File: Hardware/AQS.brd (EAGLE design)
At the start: 70 x 60 mm, 43 parts, among them IC1 BME680, IC2 CP2102N-A01-GQFN24, IC4 ESPWROOM32, J1 ESP-PROG-2X3-1.27-SHROUDED, J2 M02X5-1.27-S, J3 USB-C-16P-16P, Q1 MMDT3904, Q2 2N7002

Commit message: Finished major rework for v3.0 release
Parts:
- removed IC4: ESPWROOM32, SuperHouse-MCUs:ESPWROOM32
- added IC3: BME680, SuperHouse-Sensors:BME680
- added U$23, U$24, U$25: FIDUCIAL1X2, SuperHouse-Symbols:FIDUCIAL-1X2
- C2, C3: device SuperHouse-DiscreteSemi:C0603 -> SuperHouse-DiscreteSemi:C0805
- C5: value 10uF 50V -> 10uF
- IC1: value BME680 -> ESPWROOM32; device SuperHouse-Sensors:BME680 -> SuperHouse-MCUs:ESPWROOM32
- LED2: value WS2812B5050 -> TX/YEL; device SuperHouse-LEDs:WS2812B -> SuperHouse-LEDs:LED-0603
- LED5: value TX/YEL -> WS2812B5050; device SuperHouse-LEDs:LED-0603 -> SuperHouse-LEDs:WS2812B
- R1: value 10K -> 1K
- R10: value 5.1K -> 10K
- R11: value 22K -> 10K
- R13: value 4K7 -> 22K
- R14: value 4K7 -> 22.1K
- R15: value 4K7 -> 47.5K
- R2: value 22.1K -> 1K
- R3: value 47.5K -> 4K7
- R5: value 10K -> 4K7
- R6: value 5.1K -> 4K7
- R7: value 10K -> 5.1K
- R8: value 1K -> 5.1K
- R9: value 1K -> 10K
- moved R5 69.3 mm to (63.5, 13.0), turned to 0 degrees
- moved LED5 60.2 mm to (64.0, 51.0)
- moved LED4 58.0 mm to (6.00, 51.0)
- moved R15 55.9 mm to (9.00, 25.5), turned to 270 degrees
- moved R14 55.5 mm to (9.00, 21.5), turned to 270 degrees
- moved R11 54.0 mm to (7.00, 45.0), turned to 270 degrees
- moved R6 53.7 mm to (63.5, 11.0), turned to 0 degrees
- moved R13 53.6 mm to (61.0, 45.5)
- moved R1 46.1 mm to (5.00, 29.0), turned to 90 degrees
- moved R9 46.1 mm to (40.0, 59.0), turned to 0 degrees
- moved IC1 44.1 mm to (16.5, 55.0), flipped to the bottom, turned to 0 degrees
- moved R10 35.9 mm to (2.00, 45.0), turned to 90 degrees
- moved R3 30.5 mm to (8.50, 56.5), turned to 90 degrees
- moved R7 29.2 mm to (10.0, 16.0), turned to 180 degrees
- moved R8 19.2 mm to (10.0, 10.0), turned to 180 degrees
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- renumbered C12 to C7, LED6 to LED3
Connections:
- removed net GPIO13: IC4.16, Q2.2, R4.1
- removed net GPIO2: IC4.24, LCD.DC
- removed net GPIO23: IC4.37
- removed net GPIO4: IC4.26
- removed net TFT_CIPO: IC4.31
- removed net TFT_CS: IC4.11
- removed net TFT_RESET: LCD.RES
- new net TFT_DC: IC1.24, LCD.DC
- new net TFT_RST: IC1.26, LCD.RES
- new net WS2812B: IC1.16, Q2.2, R4.1
- net !RESET: now also IC1.3, R13.2; no longer IC4.3, R11.2
- net 3.3V: now also IC3.2, IC3.6, IC3.8, LED2.A, R13.1, R5.2, R6.2, R9.2; no longer IC1.6, IC1.8, IC4.2, LED5.A, R1.2, R11.1, R14.2, R15.2
- net 5V: now also LED5.1-VDD, R14.2, R3.2; no longer LED2.1-VDD, R13.2, R2.2
- net DTR: now also R10.1; no longer R5.1
- net GND: now also IC1.15, IC1.38, IC1.GND@4, IC3.1, IC3.5, IC3.7, LED5.3-GND, R15.1, R7.1, R8.1; no longer IC1.5, IC1.7, IC4.1, IC4.15, IC4.38, IC4.GND@4, LED2.3-GND, R10.1, R3.1, R6.1
- net GPIO0: now also IC1.25; no longer IC4.25
- net H1: now also LED4.4-DIN, R3.1; no longer LED2.4-DIN, R13.1
- net N$1: now also R9.1; no longer R1.1
- net N$10: now also R8.2; no longer R10.2
- net N$11: now also R7.2; no longer R6.2
- net N$12: now also LED4.2-DOUT, LED5.4-DIN; no longer LED2.2-DOUT, LED4.4-DIN
- net N$13: now also LED2.C, R1.2; no longer LED5.C, R9.2
- net N$2: now also R2.2; no longer R8.2
- net N$39: now also R14.1, R15.2; no longer R2.1, R3.2
- net N$7: now also R10.2; no longer R5.2
- net N$8: now also R11.2; no longer R7.2
- net PMS_RESET: now also IC1.12; no longer IC4.12
- net PMS_RX: now also IC1.28; no longer IC4.28
- net PMS_SET: now also IC1.10; no longer IC4.10
- net PMS_TX: now also IC1.27; no longer IC4.27
- net RTS: now also R11.1; no longer R7.1
- net RXD0: now also IC1.34; no longer IC4.34
- net RX_LED: now also R2.1; no longer R8.1
- net SCL: now also IC1.36, IC3.4, R6.1; no longer IC1.4, IC4.36, R14.1
- net SDA: now also IC1.33, IC3.3, R5.1; no longer IC1.3, IC4.33, R15.1
- net TFT_COPI: now also IC1.37
- net TFT_SCLK: now also IC1.30; no longer IC4.30
- net TXD0: now also IC1.35; no longer IC4.35
- net TX_LED: now also R1.1; no longer R9.1
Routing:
- net GPIO2: track 56.5 -> 0.00 mm, vias 2 -> 0
- net TFT_RST: track 0.00 -> 55.8 mm, vias 0 -> 1
- net TFT_DC: track 0.00 -> 54.1 mm, vias 0 -> 1
- net GPIO4: track 50.5 -> 0.00 mm, vias 2 -> 0
- net TFT_COPI: track 0.00 -> 32.1 mm, vias 0 -> 1
- net WS2812B: track 0.00 -> 32.0 mm, vias 0 -> 3
- net GPIO23: track 29.9 -> 0.00 mm, vias 2 -> 0
- net PMS_TX: track 43.9 -> 17.0 mm, vias 2 -> 1
- net SDA: track 59.8 -> 85.9 mm, vias 1 -> 3
- net SCL: track 68.7 -> 92.9 mm, vias 1 -> 3
- net PMS_RESET: track 38.6 -> 29.1 mm
- net PMS_RX: track 15.1 -> 21.9 mm, vias 0 -> 1
- net 3.3V: track 51.4 -> 57.1 mm
- net PMS_SET: track 20.0 -> 23.9 mm, vias 1 -> 0
- net !RESET: track 83.1 -> 85.5 mm
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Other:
- board text added: "Pin Assignments: GPIO0: Button (active low) GPIO1: USB_TX GPIO2: TFT_DC GPIO3: USB_RX GPIO4: TFT_RST GPIO13: WS2812B GPIO16: PMS_TX (RX2 of MCU) GPIO17: PMS_RX (TX2 of MCU) GPIO18: TFT_SCLK GPIO21: SDA GPIO22: SCL GPIO23: TFT_COPI GPIO25: PMS_SET GPIO27: PMS_RESET"
- board text added: "v3.0"
- board text removed: "Pin Assignments: GPIO0: Button GPIO2: TFT_DC GPIO4: TFT_RST GPIO12: Tx to PMS7003 Rx GPIO14: PMS7003 SET GPIO15: TFT_CS GPIO16: WS2812B GPIO17: Rx from PMS7003 Tx GPIO18: TFT_SCLK GPIO19: TFT_MISO GPIO23: TFT_MOSI GPIO25: SDA GPIO26: SCL GPIO27: PMS7003 RESET"
- board text removed: "v2.0"

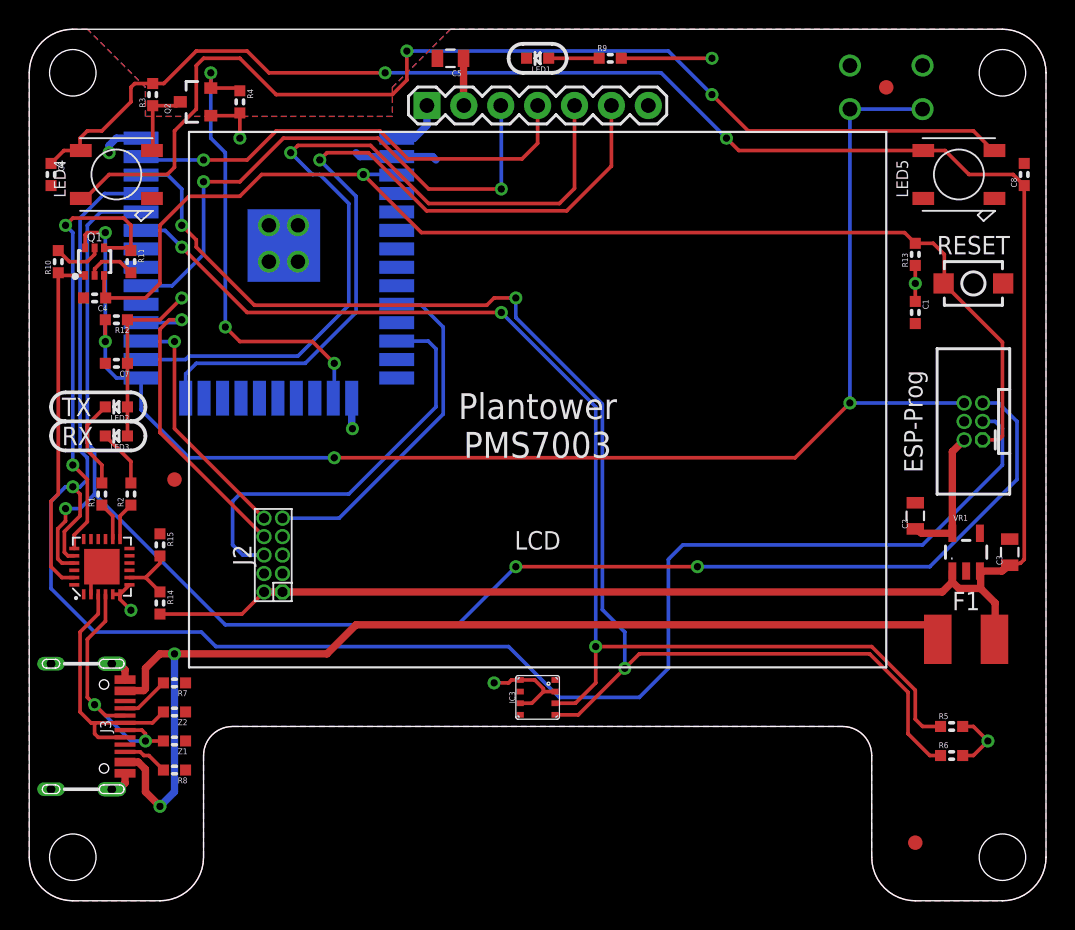
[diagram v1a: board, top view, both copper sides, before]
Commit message: Major restructure to reduce size of PCB. ERC and DRC for v3.0 release.
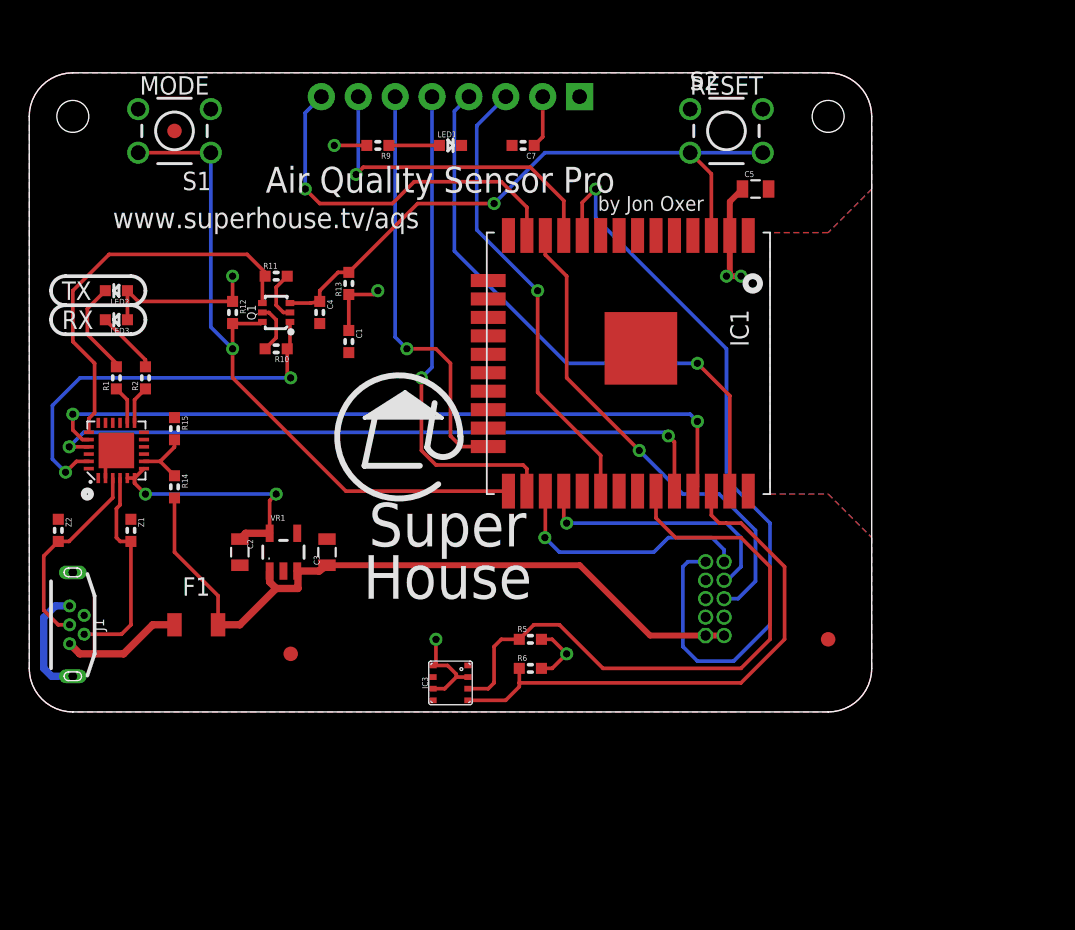
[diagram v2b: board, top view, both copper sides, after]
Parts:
- removed C6, C8: 100nF, SuperHouse-DiscreteSemi:C0603
- removed J3: USB-C-16P-16P, SuperHouse-Connectors:USB-C-16P
- removed LCD: OLED-SPI-HEADER, SuperHouse-Displays:OLED-240X240-1.3-HEADER
- removed LED4, LED5: WS2812B5050, SuperHouse-LEDs:WS2812B
- removed Q2: 2N7002, SuperHouse-DiscreteSemi:SOT23-3
- removed R3, R4: 4K7, SuperHouse-DiscreteSemi:R0603
- removed R7, R8: 5.1K, SuperHouse-DiscreteSemi:R0603
- added MOD1: OLED-SPI-CS-PINS, SuperHouse-Displays:OLED-240X240-1.54
- F1: device SuperHouse-Fuses:1812 -> SuperHouse-Fuses:1206
- J1: value ESP-PROG-2X3-1.27-SHROUDED -> USB; device SuperHouse-ESP-Prog:2X3-1.27-SHROUDED -> SuperHouse-Connectors:USB-MICROB-VERT
- S2: device SuperHouse-Switches:TACTILE_SMT_3X4X2 -> SuperHouse-Switches:TACTILE-PTH-4.5MM
- moved J1 63.6 mm to (3.00, 20.0)
- moved F1 53.0 mm to (11.5, 20.0)
- moved S1 49.1 mm to (10.0, 54.0), flipped to the top
- moved U$23 49.1 mm to (10.0, 54.0)
- moved C3 47.0 mm to (20.5, 25.0)
- moved VR1 47.0 mm to (17.5, 25.0)
- moved C2 46.6 mm to (14.5, 25.0), turned to 270 degrees
- moved U$24 46.3 mm to (55.0, 19.0)
- moved U$25 44.9 mm to (18.0, 18.0)
- moved C1 39.1 mm to (22.0, 39.5)
- moved R13 39.1 mm to (22.0, 43.5)
- moved IC1 38.5 mm to (51.0, 38.0), flipped to the top, turned to 270 degrees
- moved C7 31.8 mm to (34.0, 53.0)
- moved J2 30.5 mm to (47.2, 21.8), flipped to the bottom
- moved R5 29.6 mm to (34.5, 19.0)
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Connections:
- net PMS_RESET renamed IO27_PMS_RESET
- net PMS_RX renamed IO17_PMS_RX
- net PMS_SET renamed IO25_PMS_SET
- net PMS_TX renamed IO16_PMS_TX
- net SCL renamed IO22_SCL
- net SDA renamed IO21_SDA
- removed net H1: LED4.4-DIN, Q2.3, R3.1
- removed net N$10: J3.B5, R8.2
- removed net N$11: J3.A5, R7.2
- removed net N$12: LED4.2-DOUT, LED5.4-DIN
- removed net TFT_COPI: IC1.37, LCD.SDA
- removed net TFT_DC: IC1.24, LCD.DC
- removed net TFT_RST: IC1.26, LCD.RES
- removed net TFT_SCLK: IC1.30, LCD.SCK
- removed net VIN: F1.1, J3.A4B9, J3.A9B4
- removed net WS2812B: IC1.16, Q2.2, R4.1
- new net IO13: IC1.16
- new net IO14_TFT_BLK: IC1.13, MOD1.BLK
- new net IO18_SCLK: IC1.30, MOD1.SCK
- new net IO23_COPI: IC1.37, MOD1.COPI
- new net IO26_TFT_CS: IC1.11, MOD1.CS
- new net IO2_TFT_DC: IC1.24, MOD1.DC
- new net IO4_TFT_RST: IC1.26, MOD1.RES
- new net N$3: F1.1, J1.1
- net !RESET: now also S2.3, S2.4; no longer J1.1, S2.2
- net 3.3V: now also MOD1.VCC; no longer J1.2, LCD.VCC, Q2.1, R4.2
- net 5V: no longer C6.1, C8.1, LED4.1-VDD, LED5.1-VDD, R3.2
- net D+: now also J1.3; no longer J3.A6, J3.B6
- net D-: now also J1.2; no longer J3.A7, J3.B7
- net GND: now also J1.5, J1.POST1, J1.POST2, MOD1.GND, S2.2; no longer C6.2, C8.2, J1.4, J3.A12B1, J3.A1B12, J3.FIX1, J3.FIX2, J3.FIX3, J3.FIX4, LCD.GND, LED4.3-GND, LED5.3-GND, R7.1, R8.1
- net GPIO0: no longer J1.6
- net RXD0: no longer J1.5
- net TXD0: no longer J1.3
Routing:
- net 5V: track 167.7 -> 50.6 mm, vias 2 -> 0
- net N$12: track 76.4 -> 0.00 mm, vias 2 -> 0
- net VIN: track 76.1 -> 0.00 mm, vias 2 -> 0
- net TXD0: track 121.9 -> 50.6 mm, vias 1 -> 2
- net RXD0: track 108.4 -> 47.1 mm, vias 3 -> 2
- net TFT_RST: track 55.8 -> 0.00 mm, vias 1 -> 0
- net GPIO0: track 102.9 -> 47.2 mm, vias 4 -> 1
- net IO22_SCL: track 92.9 -> 37.9 mm, vias 3 -> 0
- net TFT_DC: track 54.1 -> 0.00 mm, vias 1 -> 0
- net IO21_SDA: track 85.9 -> 42.2 mm, vias 3 -> 0
- net !RESET: track 85.5 -> 43.5 mm
- net IO23_COPI: track 0.00 -> 40.7 mm, vias 0 -> 1
- net TFT_SCLK: track 39.2 -> 0.00 mm, vias 2 -> 0
- net IO4_TFT_RST: track 0.00 -> 34.0 mm, vias 0 -> 1
- net TFT_COPI: track 32.1 -> 0.00 mm, vias 1 -> 0
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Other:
- board size 70 x 60 mm -> 58 x 44 mm
- board text added: "MODE"
- board text removed: "ESP-Prog"
